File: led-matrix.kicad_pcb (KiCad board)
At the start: 2 copper layers, 87 x 66 mm, 89 parts, among them U1 MAX7219, U2 Pico

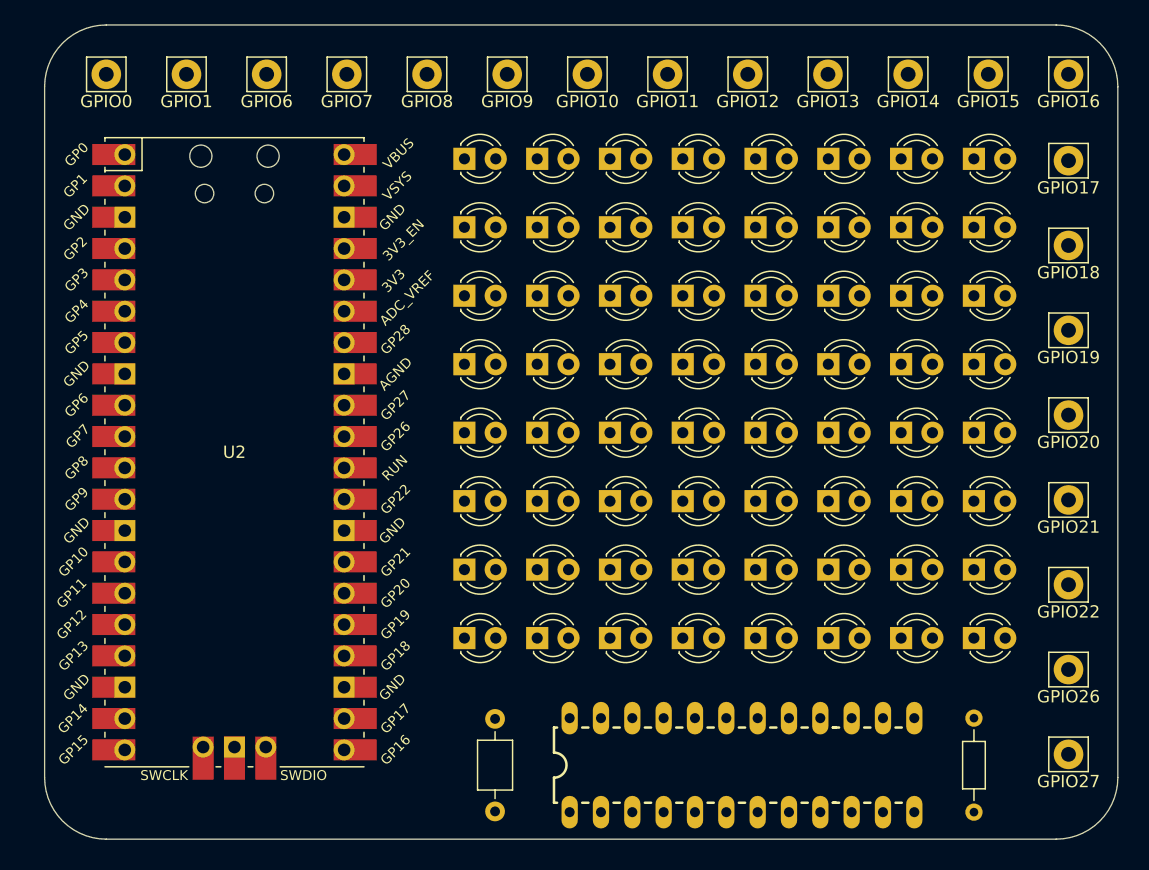
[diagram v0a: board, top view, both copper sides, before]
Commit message: feat: resize board outline
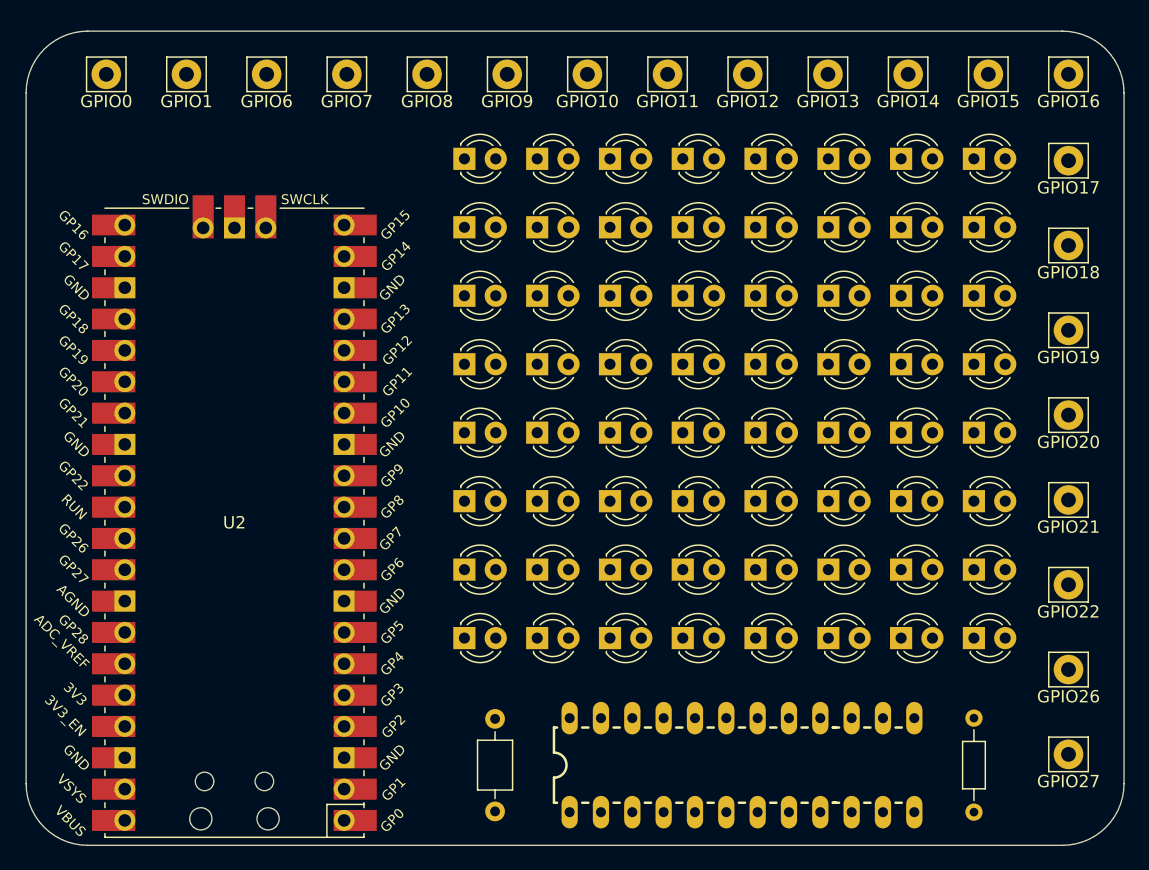
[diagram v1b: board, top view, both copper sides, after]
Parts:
- moved U2 5.71 mm to (105.4, 100.3), turned to 180 degrees
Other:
- board size 87 x 66 mm -> 89 x 66 mm

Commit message: feat: add image to pcb
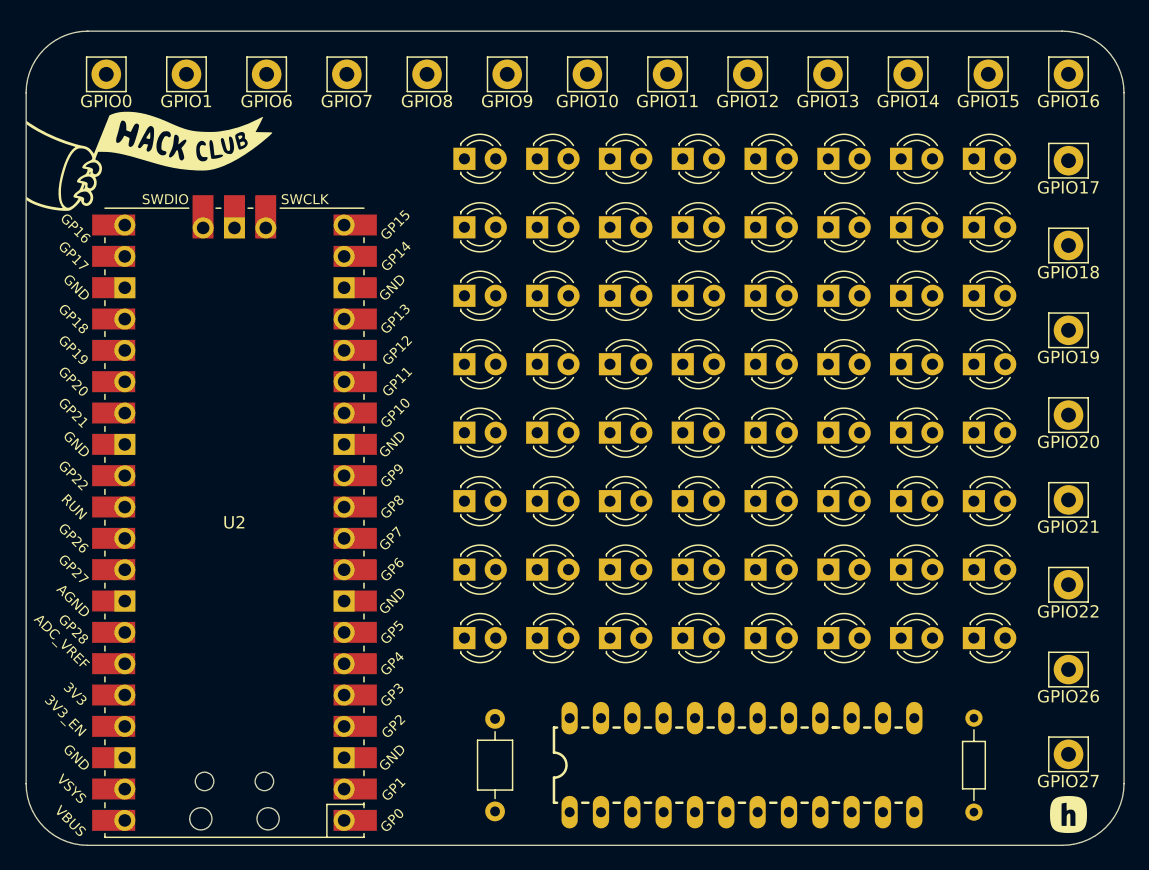
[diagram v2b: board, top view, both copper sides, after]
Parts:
- added G***: LOGO, LOGO, F.Cu at (173.0, 124.0)
- added G***: LOGO, LOGO, F.Cu at (98.5, 71.0)
- added G***: LOGO, LOGO, B.Cu at (104.5, 112.0)

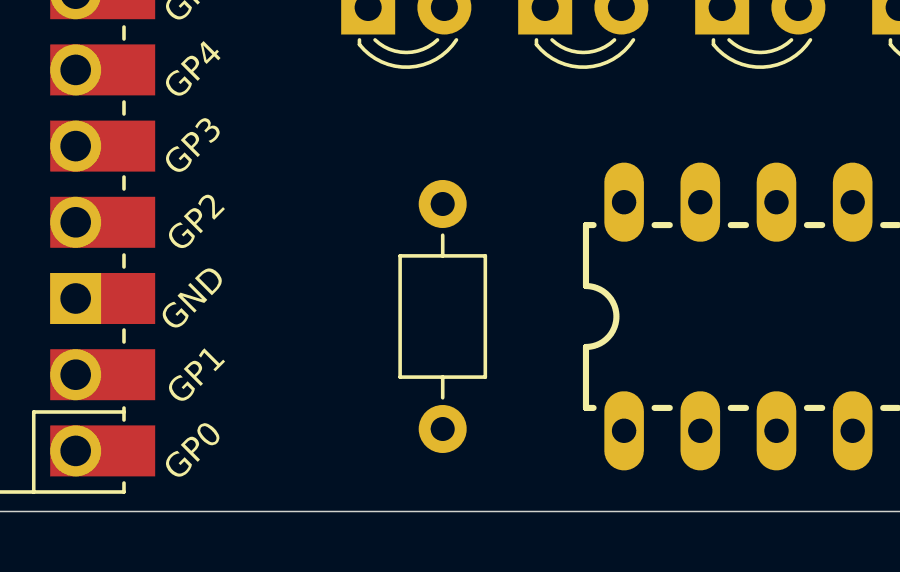
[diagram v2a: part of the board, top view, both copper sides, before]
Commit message: chore: move components for better routing
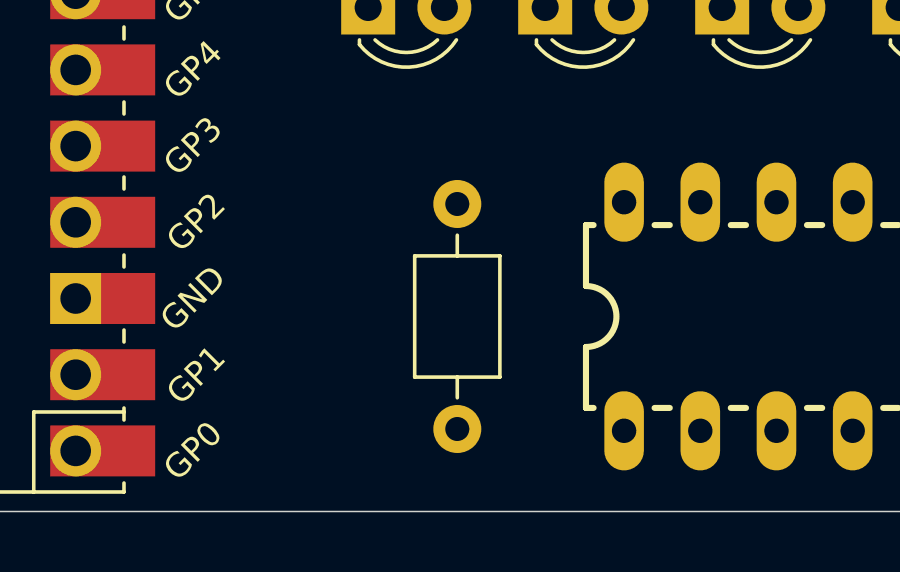
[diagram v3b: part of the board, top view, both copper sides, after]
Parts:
- moved C1 7.52 mm to (127.0, 123.8), turned to 90 degrees
- renumbered G*** to handlogo, G*** to hclogo
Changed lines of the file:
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@@
 		(layer "F.Cu")
 		(at 173 124)
-		(property "Reference" "G***"
+		(property "Reference" "hclogo"
 			(at 0 0 0)
 			(layer "F.SilkS")
@@
 	(footprint "Capacitor_THT:C_Axial_L3.8mm_D2.6mm_P7.50mm_Horizontal"
 		(layer "F.Cu")
-		(at 126.5144 116.25 -90)
+		(at 127 123.75 90)
 		(descr "C, Axial series, Axial, Horizontal, pin pitch=7.5mm, , length*diameter=3.8*2.6mm^2, http://www.vishay.com/docs/45231/arseries.pdf")
 		(tags "C Axial series Axial Horizontal pin pitch 7.5mm  length 3.8mm diameter 2.6mm")
@@
 		)
 		(property "Footprint" "Capacitor_THT:C_Axial_L3.8mm_D2.6mm_P7.50mm_Horizontal"
-			(at 0 0 -90)
+			(at 0 0 90)
 			(unlocked yes)
 			(layer "F.Fab")
@@
 		)
 		(property "Datasheet" ""
-			(at 0 0 -90)
+			(at 0 0 90)
 			(unlocked yes)
 			(layer "F.Fab")
@@
 		)
 		(property "Description" "Unpolarized capacitor"
-			(at 0 0 -90)
+			(at 0 0 90)
 			(unlocked yes)
 			(layer "F.Fab")
@@
 		(attr through_hole)
 		(fp_line
-			(start 1.73 1.42)
-			(end 5.77 1.42)
+			(start 5.77 -1.42)
+			(end 1.73 -1.42)
 			(stroke
 				(width 0.12)
@@
 		)
 		(fp_line
-			(start 5.77 1.42)
-			(end 5.77 -1.42)
+			(start 1.73 -1.42)
+			(end 1.73 1.42)
 			(stroke
 				(width 0.12)
@@
 		)
 		(fp_line
-			(start 1.04 0)
-			(end 1.73 0)
+			(start 6.46 0)
+			(end 5.77 0)
 			(stroke
 				(width 0.12)
@@
 		)
 		(fp_line
-			(start 6.46 0)
-			(end 5.77 0)
+			(start 1.04 0)
+			(end 1.73 0)
 			(stroke
 				(width 0.12)
@@
 		)
 		(fp_line
-			(start 1.73 -1.42)
-			(end 1.73 1.42)
+			(start 5.77 1.42)
+			(end 5.77 -1.42)
 			(stroke
 				(width 0.12)
@@
 		)
 		(fp_line
-			(start 5.77 -1.42)
-			(end 1.73 -1.42)
+			(start 1.73 1.42)
+			(end 5.77 1.42)
 			(stroke
 				(width 0.12)
@@
 		)
 		(fp_line
-			(start -1.05 1.55)
-			(end 8.55 1.55)
+			(start 8.55 -1.55)
+			(end -1.05 -1.55)
 			(stroke
 				(width 0.05)
@@
 		)
 		(fp_line
-			(start 8.55 1.55)
-			(end 8.55 -1.55)
+			(start -1.05 -1.55)
+			(end -1.05 1.55)
 			(stroke
 				(width 0.05)
@@
 		)
 		(fp_line
-			(start -1.05 -1.55)
-			(end -1.05 1.55)
+			(start 8.55 1.55)
+			(end 8.55 -1.55)
 			(stroke
 				(width 0.05)
@@
 		)
 		(fp_line
-			(start 8.55 -1.55)
-			(end -1.05 -1.55)
+			(start -1.05 1.55)
+			(end 8.55 1.55)
 			(stroke
 				(width 0.05)
@@
 		)
 		(fp_line
-			(start 1.85 1.3)
-			(end 5.65 1.3)
+			(start 5.65 -1.3)
+			(end 1.85 -1.3)
 			(stroke
 				(width 0.1)
@@
 		)
 		(fp_line
-			(start 5.65 1.3)
-			(end 5.65 -1.3)
+			(start 1.85 -1.3)
+			(end 1.85 1.3)
 			(stroke
 				(width 0.1)
@@
 		)
 		(fp_line
-			(start 0 0)
-			(end 1.85 0)
+			(start 7.5 0)
+			(end 5.65 0)
 			(stroke
 				(width 0.1)
@@
 		)
 		(fp_line
-			(start 7.5 0)
-			(end 5.65 0)
+			(start 0 0)
+			(end 1.85 0)
 			(stroke
 				(width 0.1)
@@
 		)
 		(fp_line
-			(start 1.85 -1.3)
-			(end 1.85 1.3)
+			(start 5.65 1.3)
+			(end 5.65 -1.3)
 			(stroke
 				(width 0.1)
@@
 		)
 		(fp_line
-			(start 5.65 -1.3)
-			(end 1.85 -1.3)
+			(start 1.85 1.3)
+			(end 5.65 1.3)
 			(stroke
 				(width 0.1)
@@
 		)
 		(pad "1" thru_hole circle
-			(at 0 0 270)
+			(at 0 0 90)
 			(size 1.6 1.6)
 			(drill 0.8)
@@
 		)
 		(pad "2" thru_hole oval
-			(at 7.5 0 270)
+			(at 7.5 0 90)
 			(size 1.6 1.6)
 			(drill 0.8)
@@
 		(layer "F.Cu")
 		(at 98.5 71)
-		(property "Reference" "G***"
+		(property "Reference" "handlogo"
 			(at 0 0 0)
 			(layer "F.SilkS")

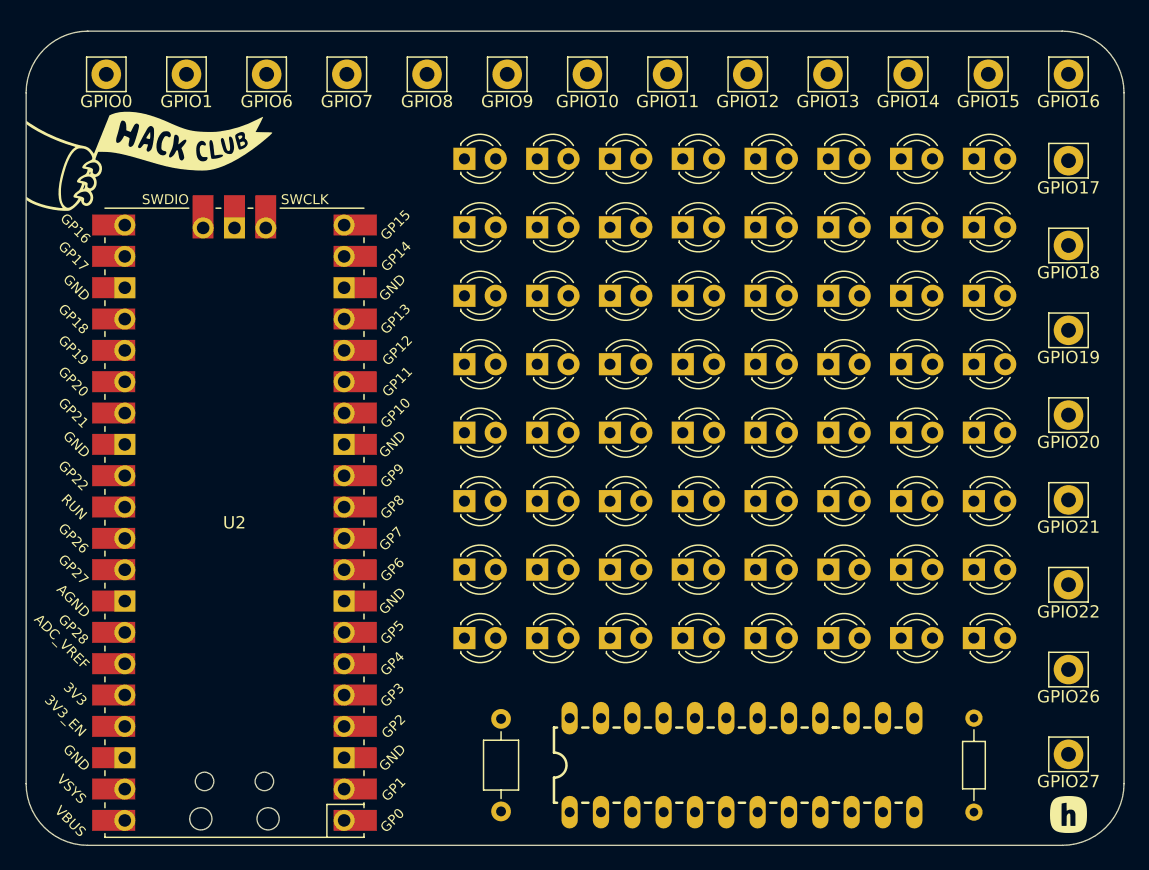
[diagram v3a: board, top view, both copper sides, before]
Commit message: feat: add routing from deeppcb
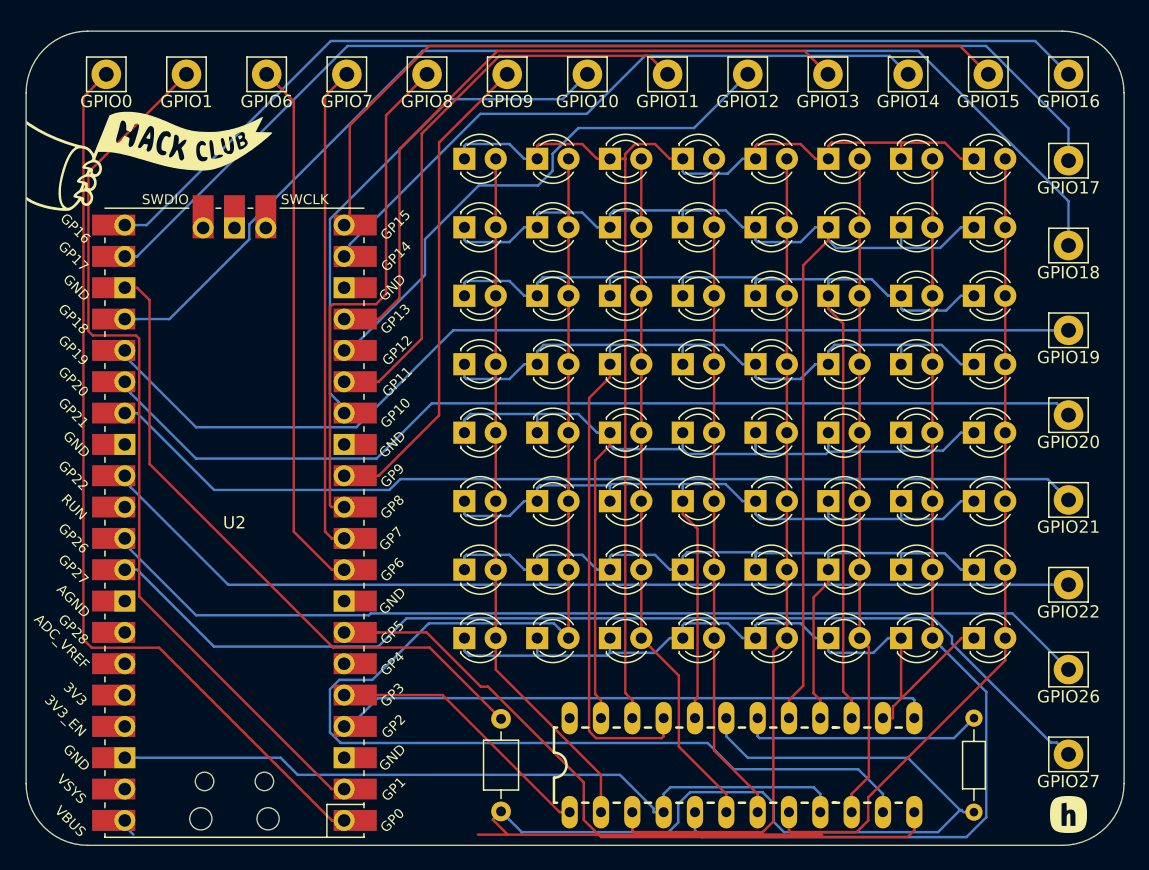
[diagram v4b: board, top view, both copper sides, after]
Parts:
- removed G***: LOGO, LOGO
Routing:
- net Net-(D10-A): track 0.00 -> 112.8 mm
- net unconnected-(C1-Pad1): track 0.00 -> 99.4 mm
- net Net-(D1-K): track 0.00 -> 97.6 mm
- net Net-(GPIO18-Pin_1): track 0.00 -> 95.3 mm
- net Net-(D10-K): track 0.00 -> 94.0 mm
- net Net-(D12-K): track 0.00 -> 91.3 mm
- net Net-(GPIO17-Pin_1): track 0.00 -> 89.4 mm
- net Net-(D11-K): track 0.00 -> 87.2 mm
- net Net-(GPIO27-Pin_1): track 0.00 -> 85.4 mm
- net Net-(GPIO16-Pin_1): track 0.00 -> 84.2 mm
- net Net-(GPIO19-Pin_1): track 0.00 -> 82.8 mm
- net Net-(GPIO20-Pin_1): track 0.00 -> 81.8 mm
- net Net-(GPIO26-Pin_1): track 0.00 -> 81.5 mm
- net Net-(D49-A): track 0.00 -> 81.2 mm
- net Net-(GPIO22-Pin_1): track 0.00 -> 80.6 mm
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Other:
- board text added: "@kcoderhtml @wanderer.archives"
